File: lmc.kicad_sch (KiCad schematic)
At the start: 0 parts

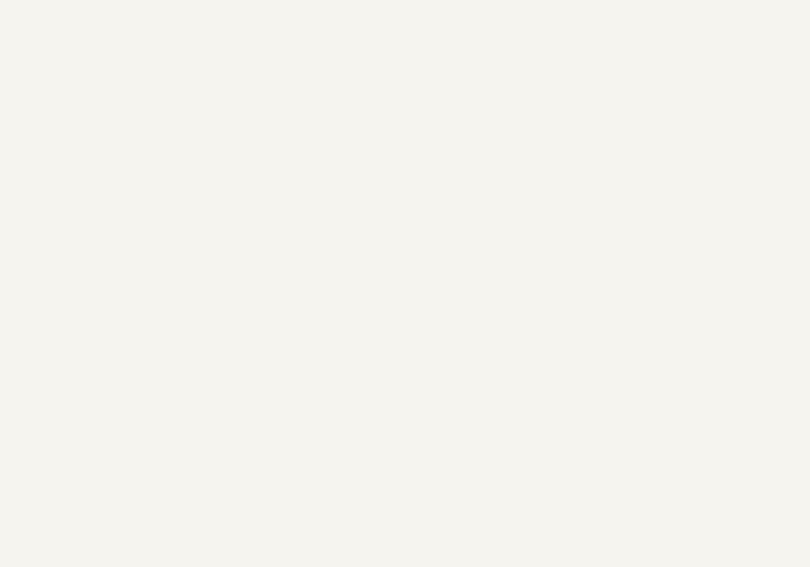
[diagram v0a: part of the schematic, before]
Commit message: schematic: continue project architecture
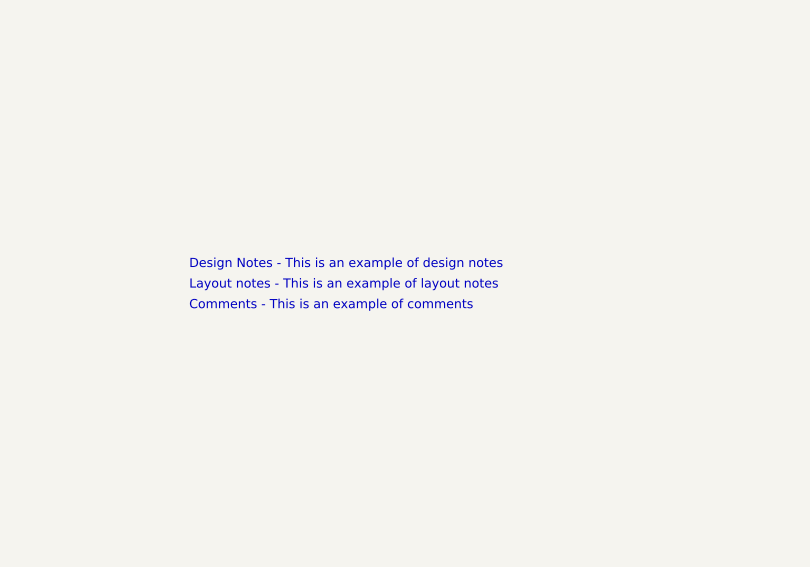
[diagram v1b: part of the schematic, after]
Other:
- note added: "Comments - This is an example of comments"
- note added: "Design Notes - This is an example of design notes"
- note added: "Layout notes - This is an example of layout notes"
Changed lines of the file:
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@@
+		)
+	)
+	(text "Comments - This is an example of comments"
+		(exclude_from_sim no)
+		(at 178.816 162.814 0)
+		(effects
+			(font
+				(size 1.016 1.016)
+				(color 0 0 194 1)
+			)
+			(justify left)
 		)
 	)
@@
 		)
 	)
+	(text "Layout notes - This is an example of layout notes"
+		(exclude_from_sim no)
+		(at 178.816 160.528 0)
+		(effects
+			(font
+				(size 1.016 1.016)
+				(color 0 255 255 1)
+			)
+			(justify left)
+		)
+	)
+	(text "Design Notes - This is an example of design notes"
+		(exclude_from_sim no)
+		(at 178.816 158.242 0)
+		(effects
+			(font
+				(size 1.016 1.016)
+				(color 255 255 0 1)
+			)
+			(justify left)
+		)
+	)

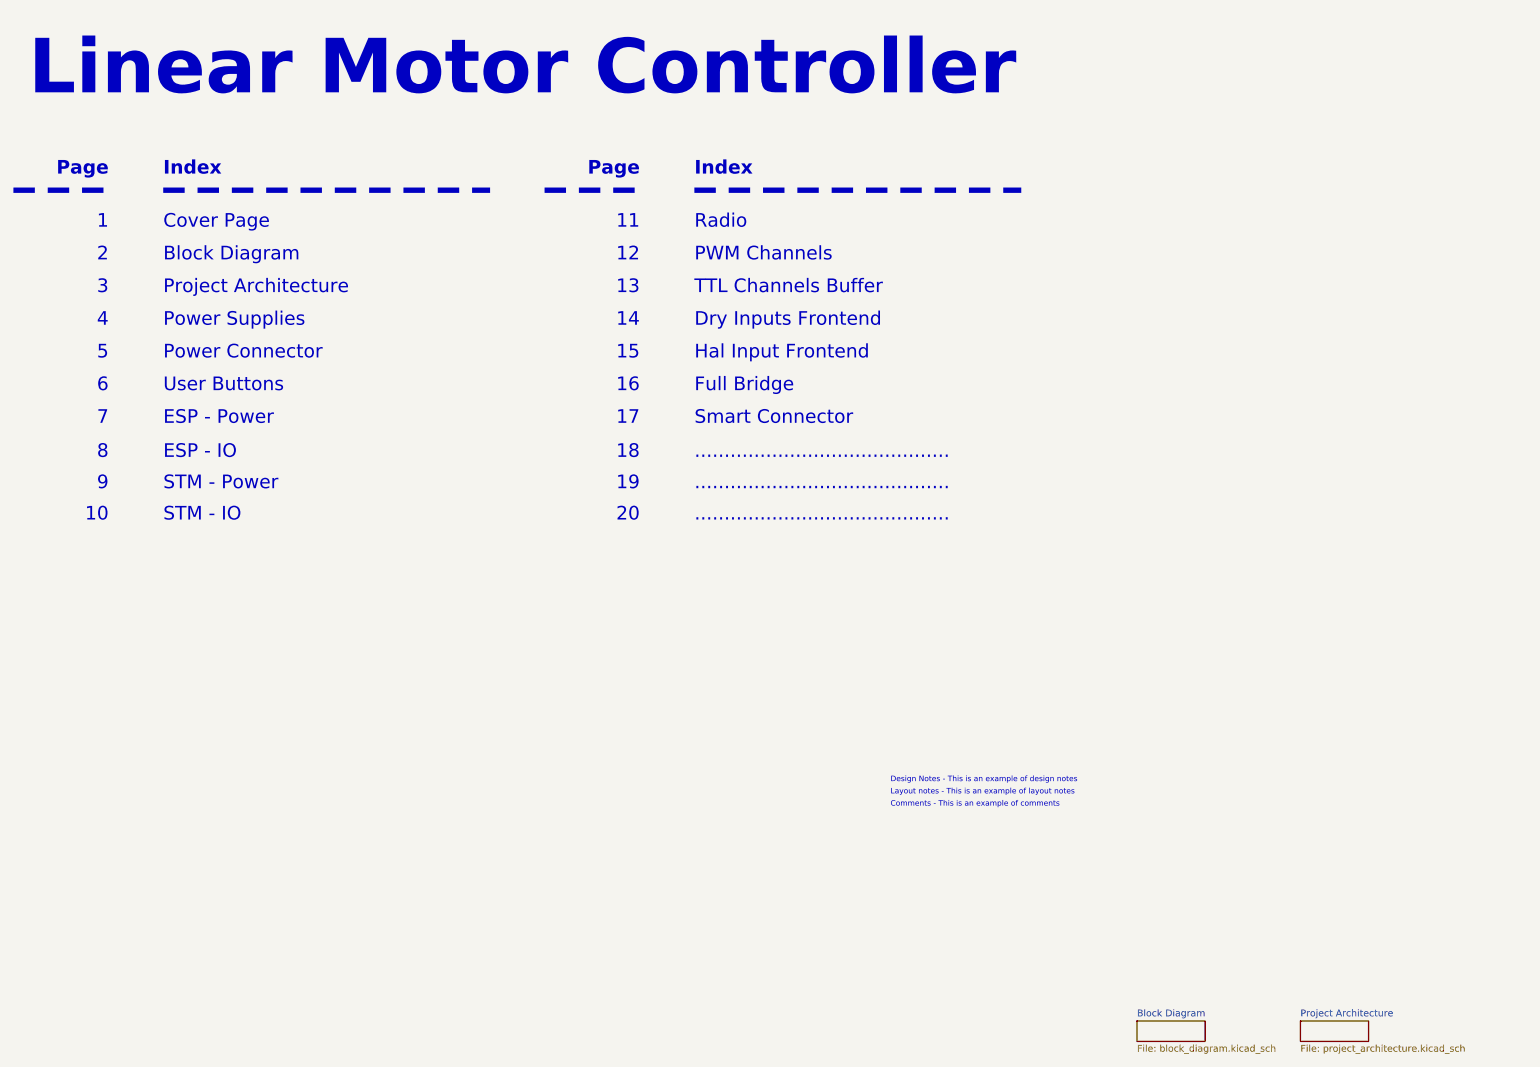
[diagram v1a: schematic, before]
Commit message: schematic: add project structure wiring
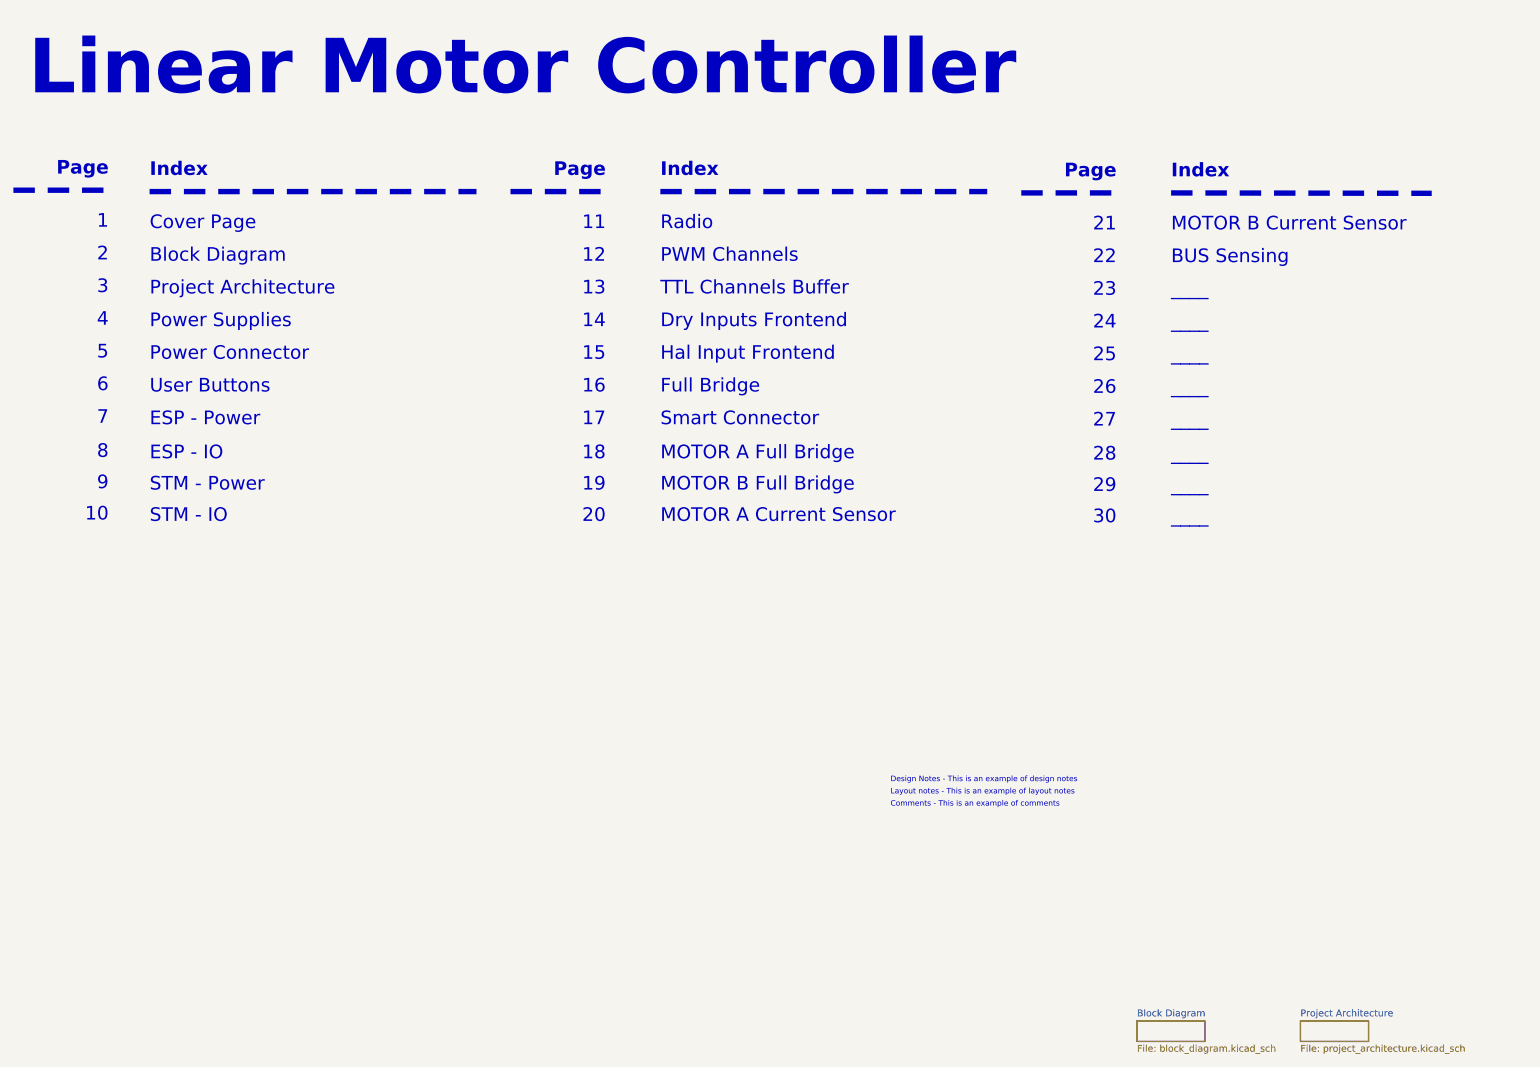
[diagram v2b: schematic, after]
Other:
- note added: "21"
- note added: "22"
- note added: "23"
- note added: "24"
- note added: "25"
- note added: "26"
- note added: "27"
- note added: "28"
- note added: "29"
- note added: "30"
- note added: "BUS Sensing"
- note added: "MOTOR A Current Sensor"
- note added: "MOTOR A Full Bridge"
- note added: "MOTOR B Current Sensor"
- note added: "MOTOR B Full Bridge"
- note added: "____"
- note removed: "..........................................."

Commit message: Add power stages
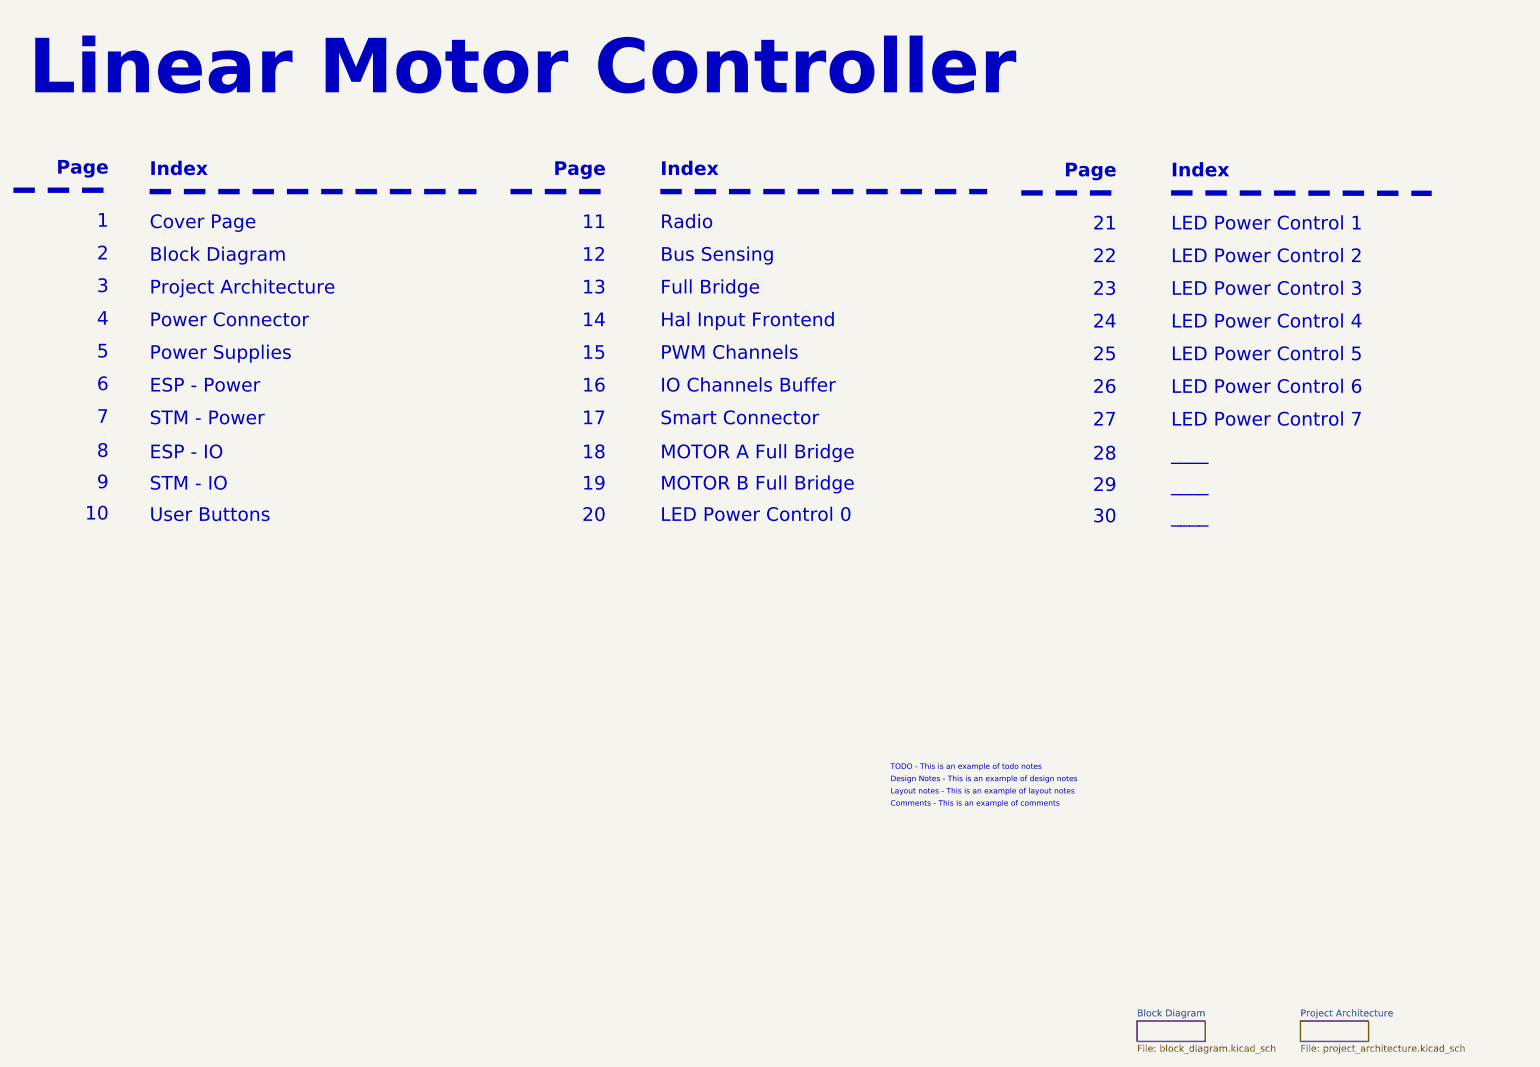
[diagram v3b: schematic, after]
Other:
- note added: "Bus Sensing"
- note added: "IO Channels Buffer"
- note added: "LED Power Control 0"
- note added: "LED Power Control 1"
- note added: "LED Power Control 2"
- note added: "LED Power Control 3"
- note added: "LED Power Control 4"
- note added: "LED Power Control 5"
- note added: "LED Power Control 6"
- note added: "LED Power Control 7"
- note added: "TODO - This is an example of todo notes"
- note removed: "BUS Sensing"
- note removed: "Dry Inputs Frontend"
- note removed: "MOTOR A Current Sensor"
- note removed: "MOTOR B Current Sensor"
- note removed: "TTL Channels Buffer"
